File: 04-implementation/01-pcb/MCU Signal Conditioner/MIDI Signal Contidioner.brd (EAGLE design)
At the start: 81.6 x 38.1 mm, 38 parts, among them J2 ARDUINO-CONN-8X2, J3 ARDUINO-CONN-8X2, U3 74LVC4245A, U4 24CS01, U5 PI6ULS5V9515A, U6 MCP1700-SOT89, X1 SSW-107-02-S-D, X2 SSW-107-02-S-D, X3 SSW-107-02-S-D, X4 SSW-107-02-S-D, X5 MINI-USB-SHIELD-32005-201

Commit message: Change signal conditioner board to 3.3V rail.
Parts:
- removed C1, C2, C4: 100n, rcl:C0805
- removed R1, R2: 0, rcl:R0805
- removed R10, R11, R12, R9: 2.2K, rcl:R0805
- removed R13, R15, R17, R19: 10K, rcl:R0805
- removed R14, R16, R18, R20: 20K, rcl:R0805
- removed U3: 74LVC4245A, MIDI Signal Conditioner Parts:74LVC4245A-SO24
- removed U5: PI6ULS5V9515A, MIDI Signal Conditioner Parts:PI6ULS5V9515A-SO8
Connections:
- removed net BIN14: J3.P$1
- removed net BIN15: J3.P$3
- removed net BIN16: J3.P$5
- removed net BIN17: J3.P$7
- removed net DI1-3V: J3.P$8, R19.1, R20.2
- removed net DI1-5V: R19.2, X4.3, X4.4
- removed net DI2-3V: J3.P$6, R17.1, R18.2
- removed net DI2-5V: R17.2, X4.5, X4.6
- removed net DI3-3V: J3.P$4, R15.1, R16.2
- removed net DI3-5V: R15.2, X4.7, X4.8
- removed net DI4-3V: J3.P$2, R13.1, R14.2
- removed net DI4-5V: R13.2, X4.10, X4.9
- removed net DO1-5V: U3.10, X3.3, X3.4
- removed net DO2-5V: U3.9, X3.5, X3.6
- removed net DO3-5V: U3.8, X3.7, X3.8
- removed net DO4-5V: U3.7, X3.10, X3.9
- removed net DO5-5V: U3.6, X2.3, X2.4
- removed net DO6-5V: U3.5, X2.5, X2.6
- removed net DO7-5V: U3.4, X2.7, X2.8
- removed net DO8-5V: U3.3, X2.10, X2.9
- new net DI1: J3.P$8, X3.3, X3.4, X4.3, X4.4
- new net DI2: J3.P$7, X3.5, X3.6, X4.5, X4.6
- new net DI3: J3.P$6, X3.7, X3.8, X4.7, X4.8
- new net DI4: J3.P$5, X3.10, X3.9, X4.10, X4.9
- new net DO1: J3.P$4, X2.3, X2.4
- new net DO2: J3.P$3, X2.5, X2.6
- new net DO3: J3.P$2, X2.7, X2.8
- new net DO4: J3.P$1, X2.10, X2.9
- net +3V3: now also X2.1, X2.14, X3.1, X3.14, X4.1, X4.14; no longer C2.1, C4.1, R10.2, R11.2, R12.2, R9.2, U3.23, U3.24, U5.8
- net +5V: no longer C1.1, U3.1, X2.1, X2.14, X3.1, X3.14, X4.1, X4.14
- net DO1-3V: no longer U3.14
- net DO2-3V: no longer U3.15
- net DO3-3V: no longer U3.16
- net DO4-3V: no longer U3.17
- net DO5-3V: no longer U3.18
- net DO6-3V: no longer U3.19
- net DO7-3V: no longer U3.20
- net DO8-3V: no longer U3.21
- net GND: no longer C1.2, C2.2, C4.2, R14.1, R16.1, R18.1, R20.1, U3.11, U3.12, U3.13, U3.2, U3.22, U5.4
- net SCL: no longer R1.2, R12.1, U5.7
- net SCL-O: no longer R1.1, R9.1, U5.2
- net SDA: no longer R10.1, R2.2, U5.6
- net SDA-O: no longer R11.1, R2.1, U5.3

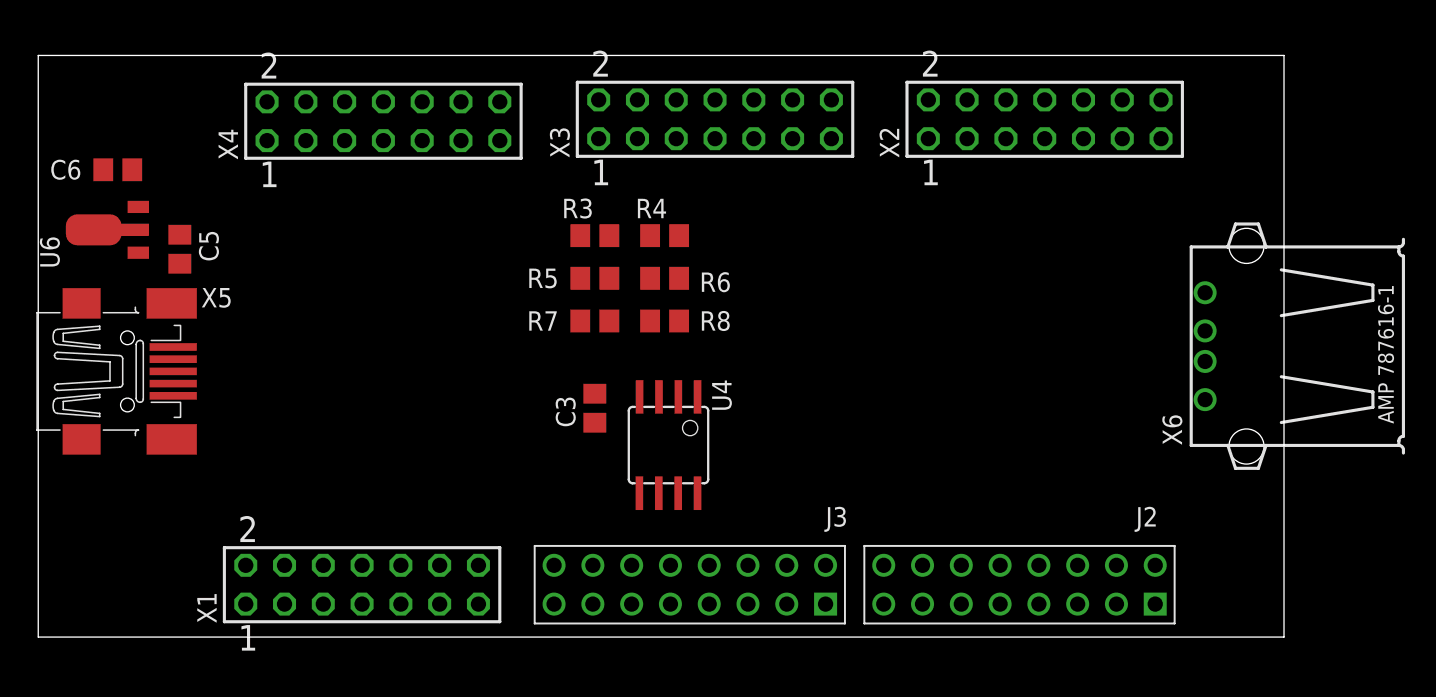
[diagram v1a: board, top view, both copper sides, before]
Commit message: Update signal conditioner.
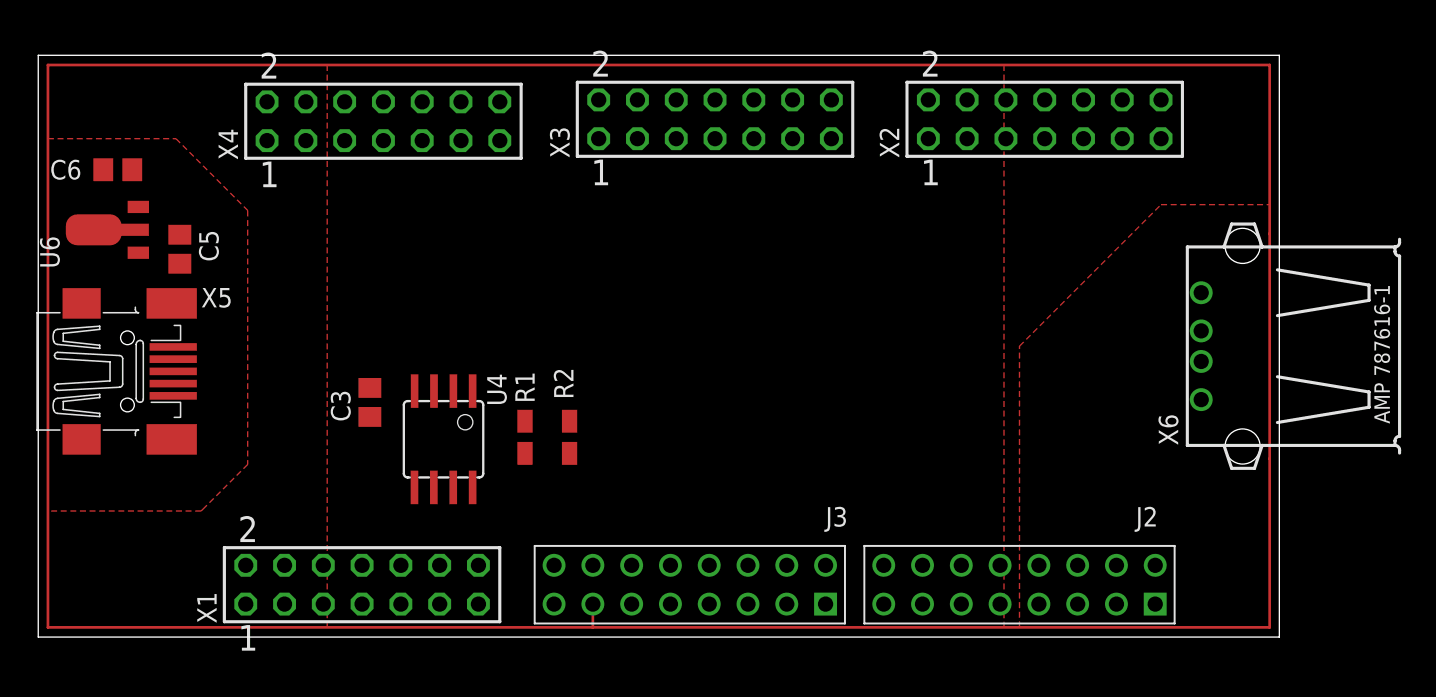
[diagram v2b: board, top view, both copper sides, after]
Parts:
- removed R3, R4, R5, R6, R7, R8: 10K, rcl:R0805
- added R1, R2: 2.2K, rcl:R0805W
- moved C3 14.7 mm to (21.7, 15.4)
- moved U4 14.7 mm to (26.5, 13.0)
- moved X6 0.25 mm to (89.2, 19.1)
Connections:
- removed net DO1-3V: J2.P$16
- removed net DO2-3V: J2.P$14
- removed net DO3-3V: J2.P$12
- removed net DO4-3V: J2.P$10
- removed net DO5-3V: J2.P$8
- removed net DO6-3V: J2.P$6
- removed net DO7-3V: J2.P$4
- removed net DO8-3V: J2.P$2
- removed net N$1: R3.1, R4.2, U4.1
- removed net N$2: R5.1, R6.2, U4.2
- removed net N$3: R7.1, R8.2, U4.3
- removed net SCL-O: X1.11, X1.12, X1.3, X1.4
- removed net SDA-O: X1.10, X1.5, X1.6, X1.9
- net +3V3: now also R1.1, R2.1; no longer R3.2, R5.2, R7.2
- net GND: now also U4.1, U4.2, U4.3; no longer R4.1, R6.1, R8.1
- net SCL: now also R1.2, X1.11, X1.12
- net SDA: now also R2.2, X1.10, X1.9
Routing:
- net +5V: track 0.00 -> 235.2 mm
- added copper zone on layer 1, net +3V3
- added copper zone on layer 1, net +5V
- added copper zone on layer 16, net GND
- added copper zone on layer 1, net VBUS
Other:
- board size 81.6 x 38.1 mm -> 81.3 x 38.1 mm

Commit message: Begin placement of components. Add Eagle exclusion to .gitignore.
Begin placement of components on board to reduce board area.
Add exclusion rules for Eagle to .gitignore.
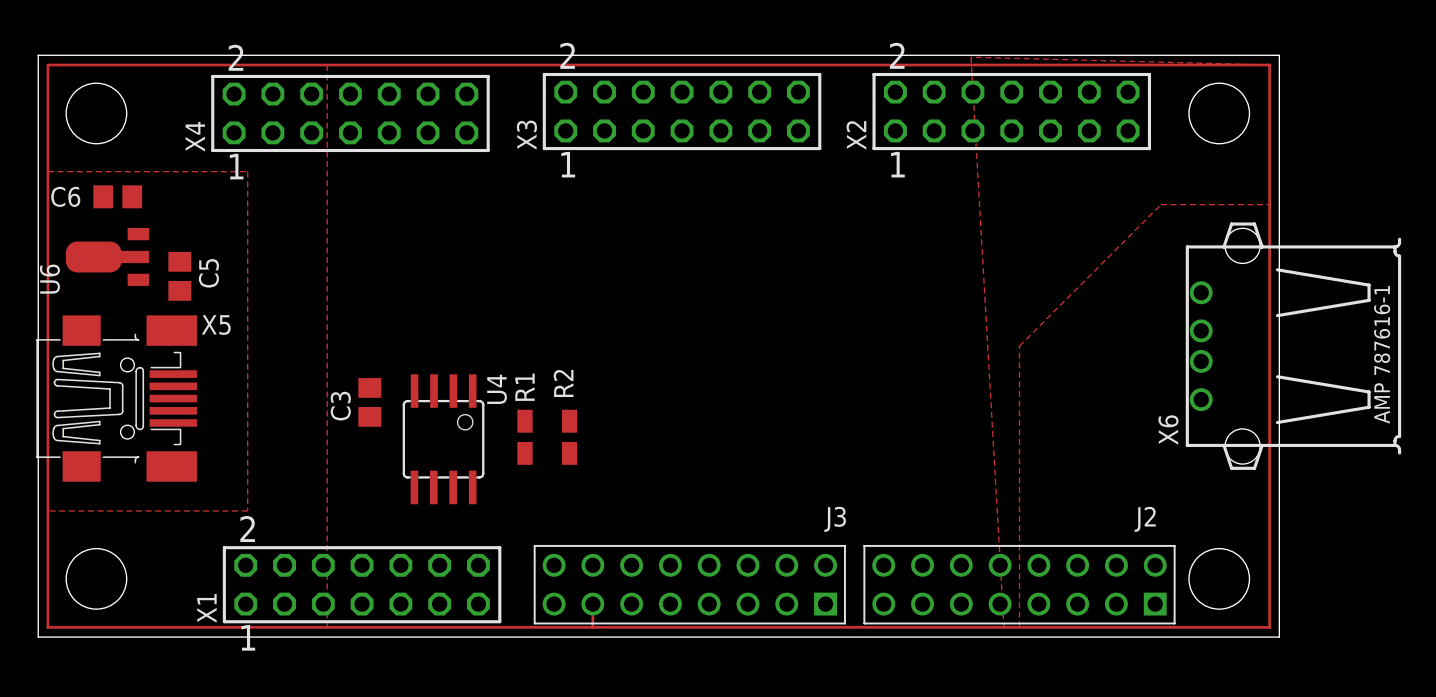
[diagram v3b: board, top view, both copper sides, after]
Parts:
- moved X4 2.22 mm to (20.4, 34.3)
- moved X2 2.22 mm to (63.8, 34.4)
- moved X3 2.22 mm to (42.2, 34.4)
- moved U6 1.78 mm to (4.57, 24.9)
- moved X5 1.78 mm to (5.84, 15.6)
- moved C5 1.78 mm to (9.27, 23.6)
- moved C6 1.78 mm to (5.21, 28.8)

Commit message: Complete initial placement of components.
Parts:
- moved C6 11.9 mm to (15.0, 22.1), turned to 270 degrees
- moved X2 7.04 mm to (60.5, 28.2)
- moved X3 7.04 mm to (38.9, 28.2)
- moved X4 7.04 mm to (17.1, 28.1)
- moved X6 4.02 mm to (85.9, 16.8)
- moved J2 3.30 mm to (69.8, 2.16)
- moved J3 3.30 mm to (48.3, 2.16)
- moved X1 3.30 mm to (17.9, 3.43)
- moved R2 3.18 mm to (32.0, 14.6)
- moved R1 3.18 mm to (29.1, 14.6)
- moved U4 3.18 mm to (23.7, 14.5)
- moved C3 2.65 mm to (19.2, 14.6)
- moved X5 2.29 mm to (5.84, 13.3)
- moved U6 2.29 mm to (4.57, 22.6)
- moved C5 1.52 mm to (9.27, 22.1)
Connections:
- net GND: now also X5.M1, X5.M2, X5.M3, X5.M4
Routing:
- net +5V: track 235.2 -> 216.2 mm
- net DI4: track 0.00 -> 5.08 mm
- net DI3: track 0.00 -> 5.08 mm
- net DI2: track 0.00 -> 5.08 mm
- net DI1: track 0.00 -> 5.08 mm
- net DO4: track 0.00 -> 2.54 mm
- net DO3: track 0.00 -> 2.54 mm
- net DO2: track 0.00 -> 2.54 mm
- net DO1: track 0.00 -> 2.54 mm
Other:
- board size 81.3 x 38.1 mm -> 78 x 31.9 mm

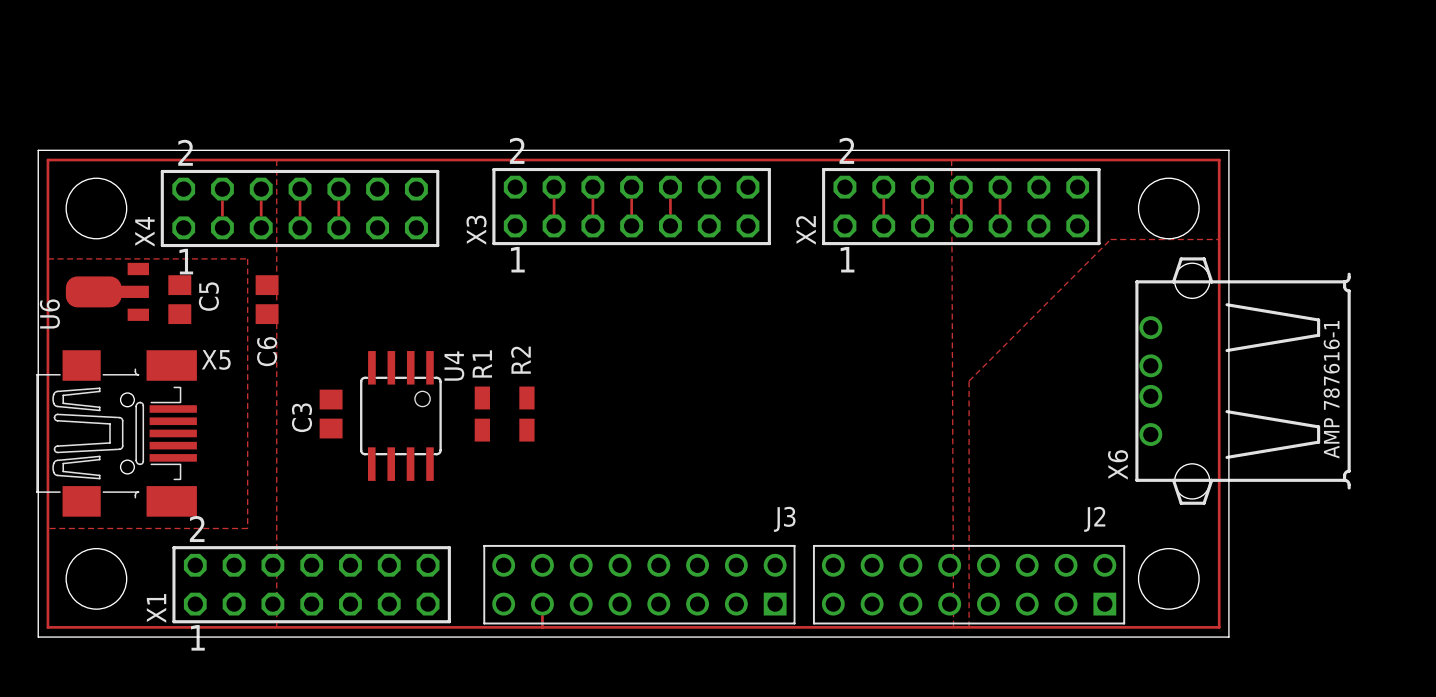
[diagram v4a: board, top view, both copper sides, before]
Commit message: Update requirements analysis. Complete first pass at signal conditioner board. Add power analysis.
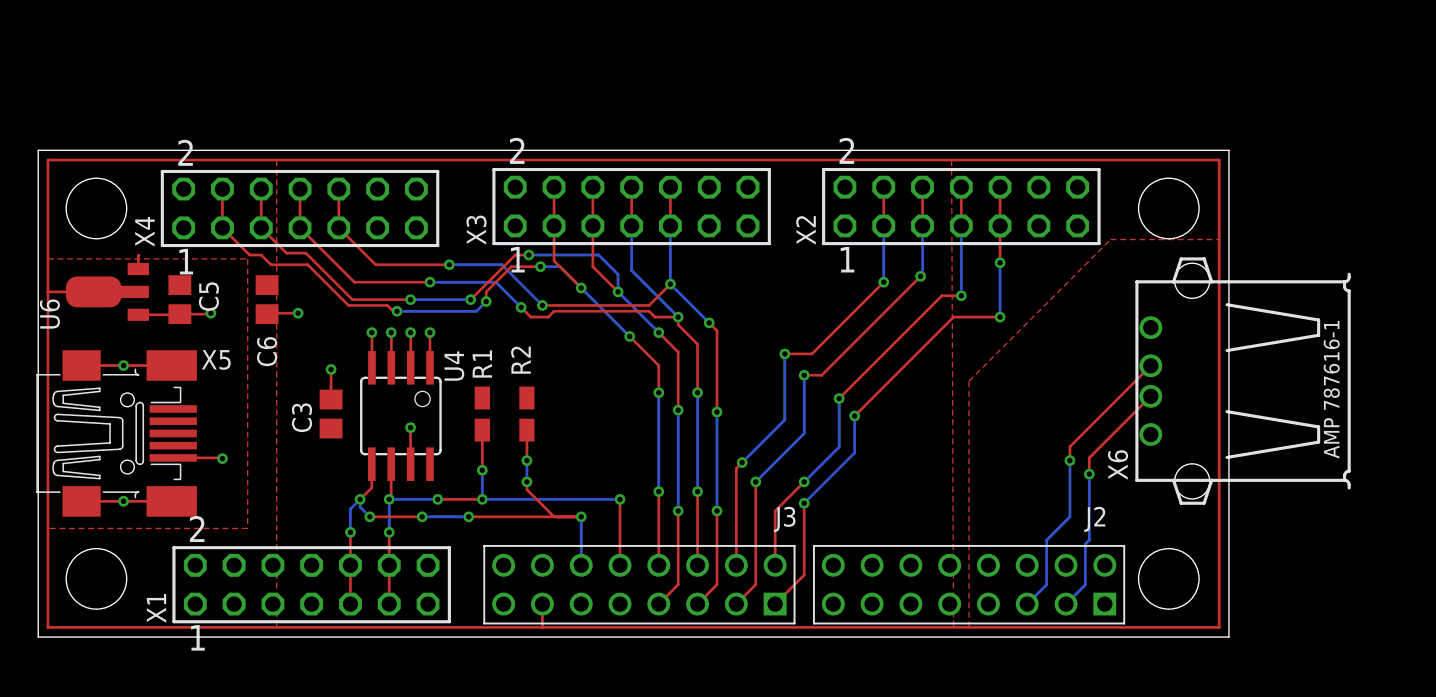
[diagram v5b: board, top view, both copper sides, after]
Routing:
- net DI2: track 5.08 -> 60.9 mm, vias 0 -> 7
- net DI1: track 5.08 -> 58.1 mm, vias 0 -> 7
- net DI3: track 5.08 -> 56.6 mm, vias 0 -> 5
- net DI4: track 5.08 -> 56.0 mm, vias 0 -> 6
- net SDA: track 0.00 -> 38.0 mm, vias 0 -> 8
- net GND: track 0.00 -> 35.5 mm, vias 0 -> 11
- net SCL: track 0.00 -> 33.2 mm, vias 0 -> 6
- net DO4: track 2.54 -> 35.2 mm, vias 0 -> 4
- net DO2: track 2.54 -> 33.0 mm, vias 0 -> 3
- net DO3: track 2.54 -> 30.6 mm, vias 0 -> 3
- net DO1: track 2.54 -> 29.8 mm, vias 0 -> 3
- net USB-D+: track 0.00 -> 19.0 mm, vias 0 -> 1
- net USB-D-: track 0.00 -> 15.9 mm, vias 0 -> 1
- net +5V: track 216.2 -> 219.2 mm
- net +3V3: track 0.00 -> 0.94 mm

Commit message: Complete initial placement of signal conditioning board (5V).
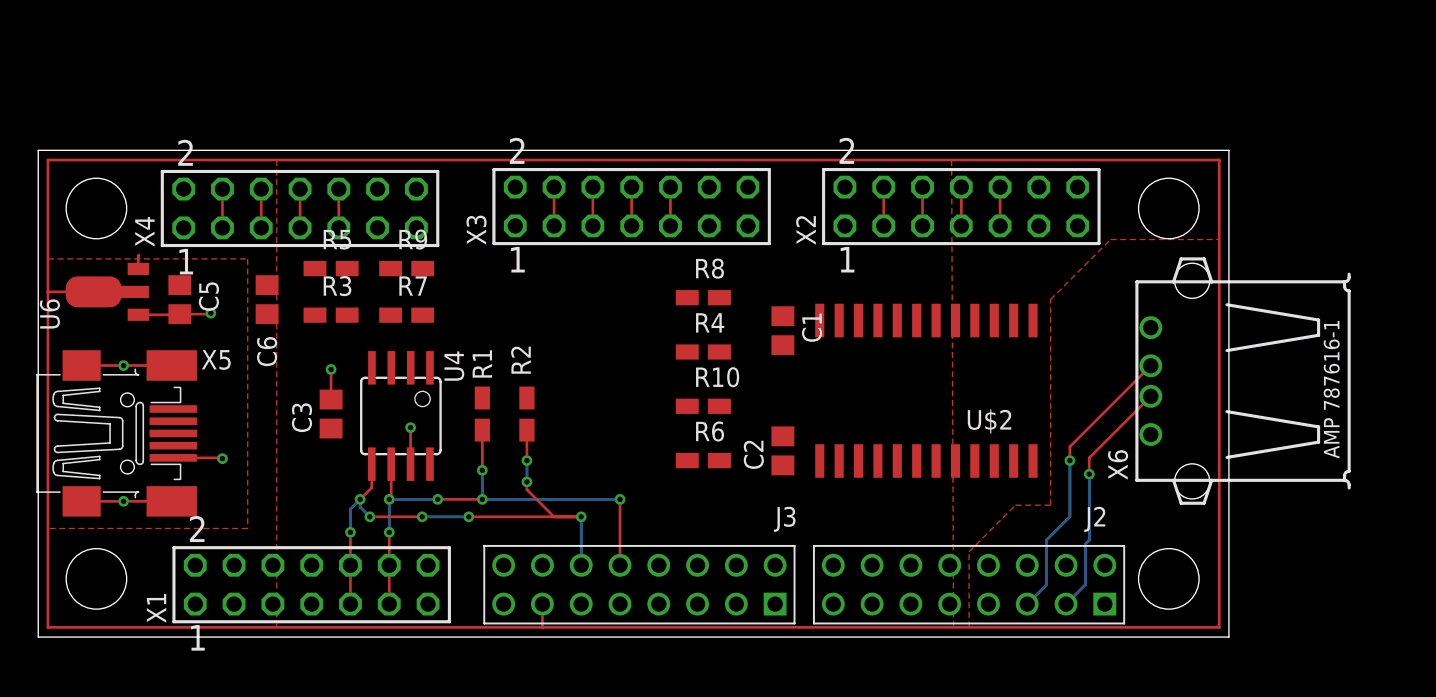
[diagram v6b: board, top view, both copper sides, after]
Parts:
- added C1, C2: 100n, rcl:C0805
- added R10, R4, R6, R8: 20K, rcl:R0805W
- added R3, R5, R7, R9: 10K, rcl:R0805W
- added U$2: 74LVC4245A, MIDI Signal Conditioner Parts:74LVC4245A-SO24
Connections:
- removed net BIN18: J3.P$9
- removed net BIN19: J3.P$11
- new net DI1-3V: J3.P$8, R3.2, R4.1
- new net DI2-3V: J3.P$7, R5.2, R6.1
- new net DI3-3V: J3.P$6, R7.2, R8.1
- new net DI4-3V: J3.P$5, R10.1, R9.2
- new net DO1-3V: J3.P$4, U$2.18
- new net DO2-3V: J3.P$3, U$2.19
- new net DO3-3V: J3.P$2, U$2.20
- new net DO4-3V: J3.P$1, U$2.21
- net +3V3: now also C1.1, U$2.23, U$2.24; no longer X1.1, X1.14, X2.1, X2.14, X3.1, X3.14, X4.1, X4.14
- net +5V: now also C2.1, U$2.1, X1.1, X1.14, X2.1, X2.14, X3.1, X3.14, X4.1, X4.14
- net DI1: now also R3.1; no longer J3.P$8
- net DI2: now also R5.1; no longer J3.P$7
- net DI3: now also R7.1; no longer J3.P$6
- net DI4: now also R9.1; no longer J3.P$5
- net DO1: now also U$2.6; no longer J3.P$4
- net DO2: now also U$2.5; no longer J3.P$3
- net DO3: now also U$2.4; no longer J3.P$2
- net DO4: now also U$2.3; no longer J3.P$1
- net GND: now also C1.2, C2.2, R10.2, R4.2, R6.2, R8.2, U$2.11, U$2.12, U$2.13, U$2.14, U$2.15, U$2.16, U$2.17, U$2.2, U$2.22
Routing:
- net DI2: track 60.9 -> 5.08 mm, vias 7 -> 0
- net DI1: track 58.1 -> 5.08 mm, vias 7 -> 0
- net DI3: track 56.6 -> 5.08 mm, vias 5 -> 0
- net DI4: track 56.0 -> 5.08 mm, vias 6 -> 0
- net DO4: track 35.2 -> 2.54 mm, vias 4 -> 0
- net DO2: track 33.0 -> 2.54 mm, vias 3 -> 0
- net DO3: track 30.6 -> 2.54 mm, vias 3 -> 0
- net DO1: track 29.8 -> 2.54 mm, vias 3 -> 0
- net GND: track 35.5 -> 24.3 mm, vias 11 -> 6
